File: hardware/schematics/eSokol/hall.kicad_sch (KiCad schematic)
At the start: 4 parts

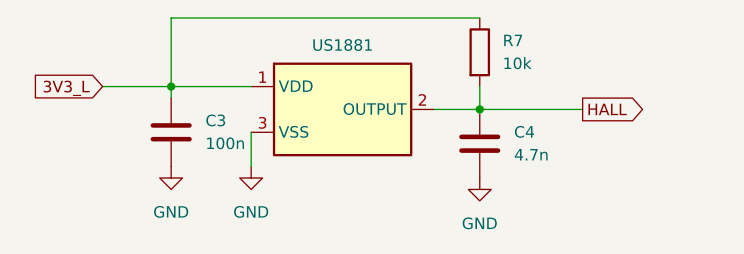
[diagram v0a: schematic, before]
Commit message: hardware: schematics: Fix improper NMOS placement, misc minor fixes
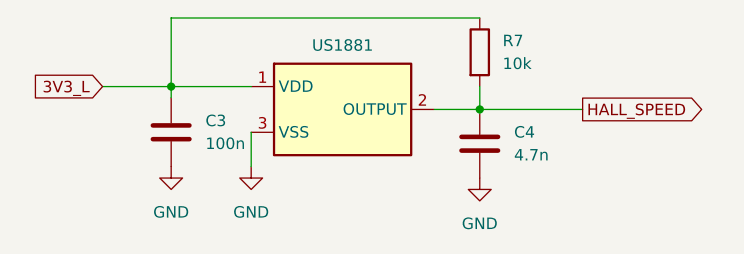
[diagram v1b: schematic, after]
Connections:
- net HALL renamed HALL_SPEED
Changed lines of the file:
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@@
 		)
 	)
-	(global_label "HALL"
+	(global_label "HALL_SPEED"
 		(shape output)
 		(at 165.1 96.52 0)
